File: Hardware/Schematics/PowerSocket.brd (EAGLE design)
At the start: 100 x 80 mm, 60 parts, among them U1 ESP-32S

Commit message: Made relay and amperemeter breakout board.
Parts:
- removed R3, R4, R9: 100, rcl:R0805
- added D2, D3, D4: (no value), diode:DO-214AC
- added Q4, Q5, Q6: (no value), adafruit:SOT23
- moved Q3 247.8 mm to (68.2, 7.90), flipped to the bottom, turned to 270 degrees
- moved Q2 225.5 mm to (72.8, 9.70), flipped to the bottom, turned to 270 degrees
- moved JTAG 185.4 mm to (80.8, 2.73), turned to 180 degrees
- moved R29 163.1 mm to (63.2, 12.4), flipped to the bottom, turned to 180 degrees
- moved U$1 158.8 mm to (62.2, 13.4), turned to 90 degrees
- moved R27 158.3 mm to (63.1, 7.47), flipped to the bottom, turned to 180 degrees
- moved R25 156.4 mm to (63.3, 17.3), flipped to the bottom, turned to 180 degrees
- moved R30 153.5 mm to (58.1, 11.2), flipped to the bottom, turned to 270 degrees
- moved R26 150.1 mm to (58.1, 16.2), flipped to the bottom, turned to 270 degrees
- moved R28 149.3 mm to (58.0, 6.30), flipped to the bottom, turned to 270 degrees
- moved C8 149.1 mm to (61.6, 27.6), flipped to the bottom, turned to 270 degrees
- moved C7 145.2 mm to (63.6, 27.5), flipped to the bottom, turned to 90 degrees
- moved C10 142.1 mm to (41.3, 28.0), flipped to the bottom, turned to 270 degrees
- moved C2 139.5 mm to (75.3, 22.7), flipped to the bottom, turned to 90 degrees
- moved C9 138.3 mm to (43.5, 28.1), flipped to the bottom, turned to 90 degrees
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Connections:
- removed net N$15: Q2.2, U$4.COIL1, U$5.COIL1
- removed net N$16: Q3.1, R9.1
- removed net N$18: Q3.2, U$6.COIL1, U$7.COIL1
- new net LED1_SWITCHED: Q5.3, R7.2
- new net LED2_SWITCHED: Q4.3, R20.2
- new net LED3_SWITCHED: Q6.3, R22.2
- new net N$19: U1.38, UART.1
- net AMP1: now also U1.7; no longer U1.6
- net AMP2: now also U1.8; no longer U1.7
- net AMP3: now also U1.9; no longer U1.8
- net FLASH: now also U1.26; no longer U1.10
- net GATE1: now also Q1.1, U1.10; no longer R3.2, U1.25
- net GATE2: now also Q2.1, U1.11; no longer R4.2, U1.26
- net GATE3: now also Q3.1, U1.12; no longer R9.2, U1.37
- net GND: now also Q1.2, Q2.2, Q3.2, Q4.2, Q5.2, Q6.2; no longer U$2.COIL0, U$3.COIL0, U$4.COIL0, U$5.COIL0, U$6.COIL0, U$7.COIL0, U1.38, UART.1
- net LED1: now also Q5.1; no longer R7.2
- net LED2: now also Q4.1; no longer R20.2
- net LED3: now also Q6.1; no longer R22.2
- net N$1: now also D4.A, Q1.3, U$2.COIL0, U$3.COIL0; no longer Q1.1, R3.1
- net N$14: now also D2.A, Q2.3, U$4.COIL0, U$5.COIL0; no longer Q2.1, R4.1
- net N$6: now also D3.A, Q3.3, U$6.COIL0, U$7.COIL0; no longer Q1.2, U$2.COIL1, U$3.COIL1
- net PHASE1: now also U$2.SWCLOSED; no longer U$2.SWOPEN
- net PHASE2: now also U$4.SWCLOSED; no longer U$4.SWOPEN
- net PHASE3: now also U$6.SWCLOSED; no longer U$6.SWOPEN
- net VCC: now also D2.C, D3.C, D4.C, U$2.COIL1, U$3.COIL1, U$4.COIL1, U$5.COIL1, U$6.COIL1, U$7.COIL1; no longer Q1.3, Q2.3, Q3.3
- net VOLTMETER: now also U1.6; no longer U1.11
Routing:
- net PHASE: track 0.00 -> 96.0 mm
- net NULL: track 0.00 -> 87.5 mm
- net N$15: track 0.00 -> 53.9 mm
- net N$16: track 0.00 -> 37.3 mm
- net +5V: track 0.00 -> 33.9 mm
- net GND: track 0.00 -> 20.9 mm
- net N$18: track 0.00 -> 8.40 mm
- net N$21: track 0.00 -> 8.30 mm
- net N$20: track 0.00 -> 8.00 mm
- net N$17: track 0.00 -> 6.38 mm
- net N$23: track 0.00 -> 6.30 mm
- net N$25: track 0.00 -> 6.10 mm
- net N$8: track 0.00 -> 5.97 mm
- net N$22: track 0.00 -> 5.90 mm
- net NULL_: track 0.00 -> 5.89 mm
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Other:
- outline, holes or cut-outs redrawn

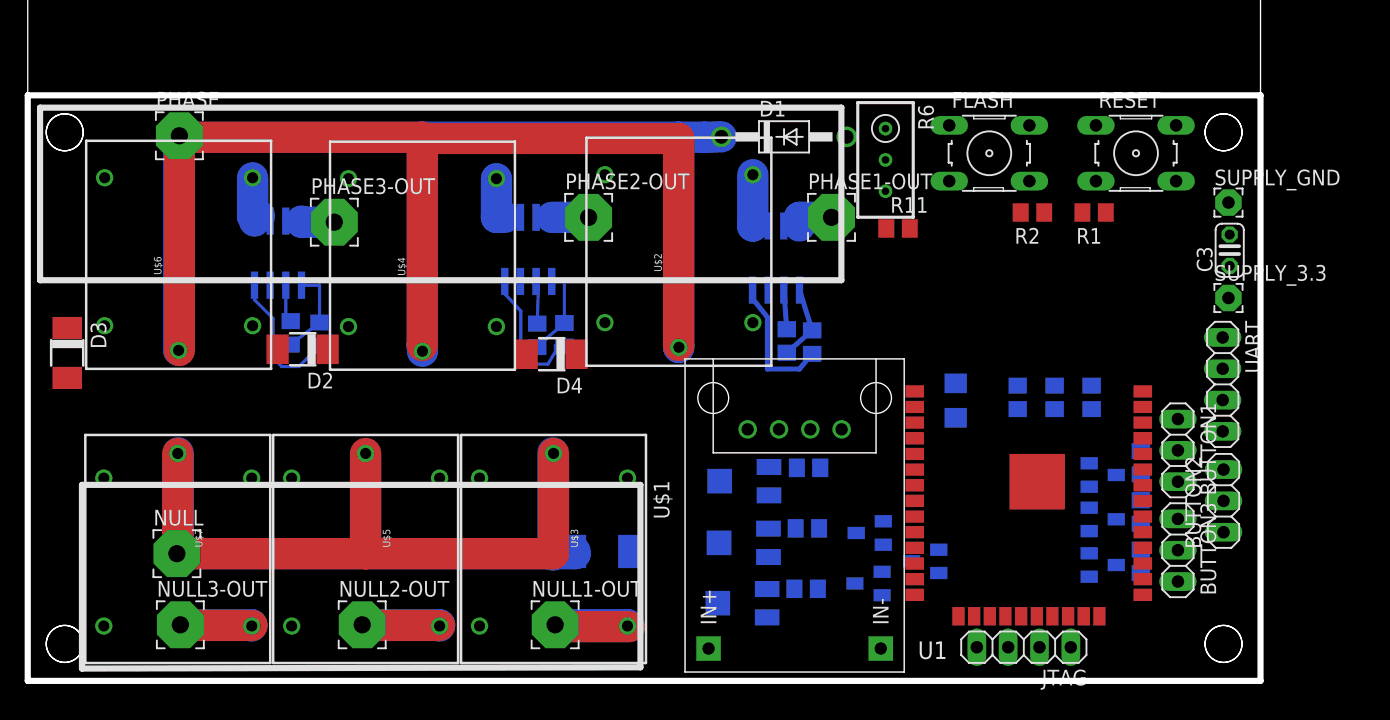
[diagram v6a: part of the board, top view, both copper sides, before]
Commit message: Routed power socket board.
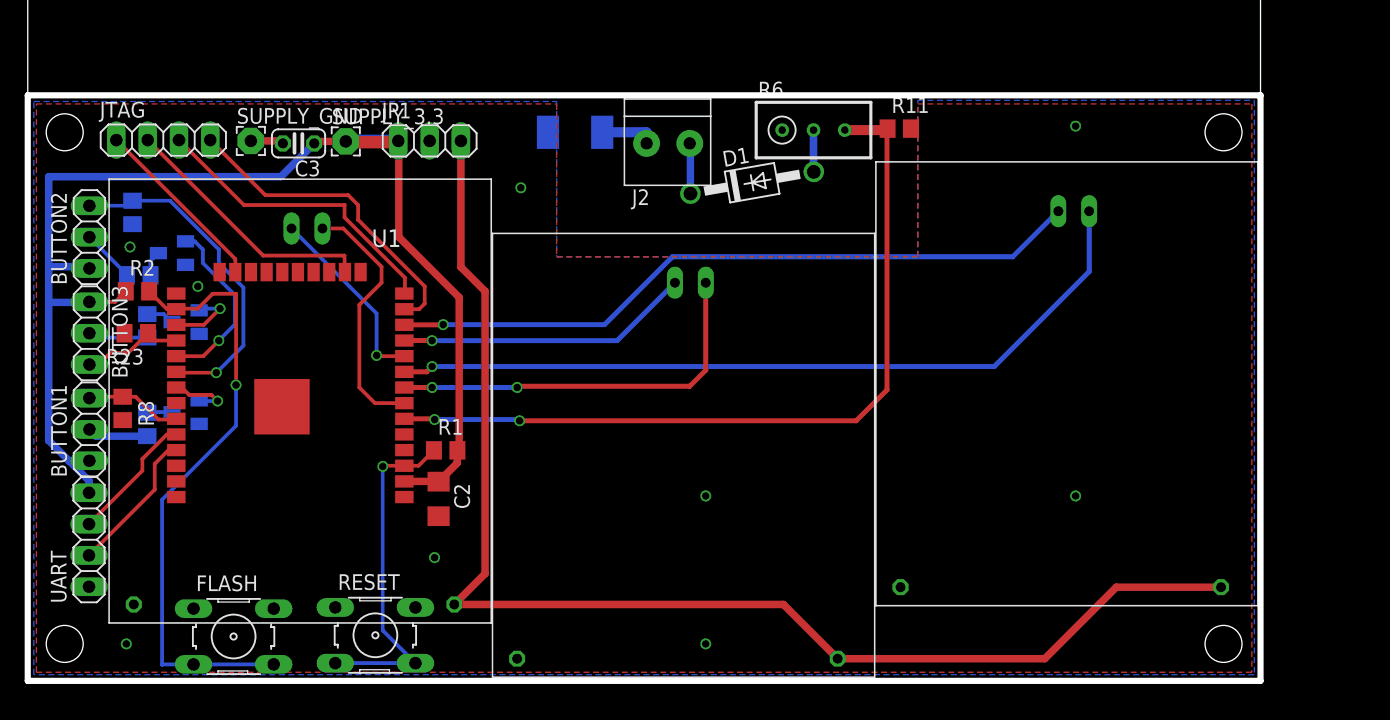
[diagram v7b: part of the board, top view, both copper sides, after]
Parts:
- removed AMP1, AMP2, AMP3: ACS712-LC, allegro-2:SOIC8
- removed C1, C7, C9: 100nF, rcl:C0805
- removed C10, C4, C8: 470nF, rcl:C0805
- removed D2, D3, D4: (no value), diode:DO-214AC
- removed NULL, NULL1-OUT, NULL2-OUT, NULL3-OUT, PHASE, PHASE1-OUT, PHASE2-OUT, PHASE3-OUT: -, wirepad:3,81/1,4
- removed Q1, Q2, Q3: (no value), adafruit:SOT23
- removed R25, R27, R29: 10K, rcl:R0805
- removed R26, R28, R30: 10K, rcl:RTRIM5X
- removed U$1: DC-DC-STEP-UP-5V, diy-modules:DC-DC-STEP-UP-5V
- removed U$5, U$6, U$7: RELAYPTH, SRD-05VDC-SL-C:SRD-05VDC-SL-C
- added J2: 1X2-3.5MM, adafruit:1X2-3.5MM
- added JP1: (no value), pinhead:1X03
- U$2, U$3, U$4: value RELAYPTH -> RELAY_BOARD; device SRD-05VDC-SL-C:SRD-05VDC-SL-C -> PowerSocket:RELAY_BOARD
- moved BUTTON2 94.5 mm to (5.00, 36.0)
- moved UART 92.8 mm to (4.97, 11.4), turned to 90 degrees
- moved BUTTON3 90.0 mm to (5.00, 28.2)
- moved BUTTON1 88.3 mm to (5.00, 20.4), turned to 90 degrees
- moved R20 83.5 mm to (9.00, 32.9), turned to 180 degrees
- moved R22 82.8 mm to (9.70, 28.8), turned to 90 degrees
- moved JTAG 81.0 mm to (11.0, 43.9), turned to 0 degrees
- moved R7 80.7 mm to (9.70, 20.8), turned to 90 degrees
- moved SUPPLY_GND 79.5 mm to (18.1, 43.8)
- moved R8 78.6 mm to (7.70, 22.1), flipped to the top, turned to 270 degrees
- moved Q4 78.5 mm to (11.7, 34.7), turned to 270 degrees
- moved Q6 77.0 mm to (12.8, 29.1), turned to 270 degrees
- moved R21 76.3 mm to (8.50, 38.0), turned to 270 degrees
- moved C3 76.0 mm to (22.0, 43.6), turned to 180 degrees
- moved Q5 74.6 mm to (12.8, 21.8), turned to 270 degrees
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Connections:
- removed net N$1: D4.A, Q1.3, U$2.COIL0, U$3.COIL0
- removed net N$10: AMP3.3, AMP3.4, PHASE3-OUT.1
- removed net N$12: AMP2.3, AMP2.4, PHASE2-OUT.1
- removed net N$13: AMP2.6, C10.1
- removed net N$14: D2.A, Q2.3, U$4.COIL0, U$5.COIL0
- removed net N$17: NULL2-OUT.1, U$5.SWOPEN
- removed net N$19: U1.38, UART.1
- removed net N$24: AMP1.6, C8.1
- removed net N$26: AMP3.6, C4.1
- removed net N$27: AMP1.3, AMP1.4, PHASE1-OUT.1
- removed net N$37: AMP3.7, R29.2
- removed net N$39: AMP2.7, R25.2
- removed net N$41: AMP1.7, R27.2
- removed net N$6: D3.A, Q3.3, U$6.COIL0, U$7.COIL0
- removed net N$8: NULL1-OUT.1, U$3.SWOPEN
- removed net NULL_: NULL3-OUT.1, U$7.SWOPEN
- removed net PHASE1: AMP1.1, AMP1.2, U$2.SWCLOSED
- removed net PHASE2: AMP2.1, AMP2.2, U$4.SWCLOSED
- removed net PHASE3: AMP3.1, AMP3.2, U$6.SWCLOSED
- net +5V: now also JP1.3, U$2.+5V, U$3.+5V, U$4.+5V; no longer AMP1.8, AMP2.8, AMP3.8, C1.1, C7.1, C9.1, U$1.5V
- net AMP1: now also U$4.AMP; no longer R27.1, R28.1
- net AMP2: now also U$3.AMP; no longer R25.1, R26.1
- net AMP3: now also U$2.AMP; no longer R29.1, R30.1
- net GATE1: now also U$4.GATE; no longer Q1.1
- net GATE2: now also U$3.GATE; no longer Q2.1
- net GATE3: now also U$2.GATE; no longer Q3.1
- net GND: now also JP1.2, U$2.GND, U$3.GND, U$4.GND, U1.38, UART.1; no longer AMP1.5, AMP2.5, AMP3.5, C1.2, C10.2, C4.2, C7.2, C8.2, C9.2, Q1.2, Q2.2, Q3.2, R26.2, R28.2, R30.2, U$1.D+, U$1.D-, U$1.GND, U$1.IN-
- net NULL: now also J2.1; no longer NULL.1, U$3.SWCOMMON, U$5.SWCOMMON, U$7.SWCOMMON
- net PHASE: now also J2.2; no longer PHASE.1, U$2.SWCOMMON, U$4.SWCOMMON, U$6.SWCOMMON
- net VCC: now also JP1.1; no longer D2.C, D3.C, D4.C, U$1.IN+, U$2.COIL1, U$3.COIL1, U$4.COIL1, U$5.COIL1, U$6.COIL1, U$7.COIL1
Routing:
- net VCC: track 0.00 -> 105.7 mm
- net PHASE: track 96.0 -> 4.07 mm
- net NULL: track 87.5 -> 4.50 mm
- net +5V: track 33.9 -> 105.9 mm
- net VOLTMETER: track 0.00 -> 65.1 mm, vias 0 -> 2
- net AMP3: track 0.00 -> 63.8 mm, vias 0 -> 1
- net GATE3: track 0.00 -> 56.9 mm, vias 0 -> 1
- net N$15: track 53.9 -> 0.00 mm
- net FLASH: track 0.00 -> 49.8 mm, vias 0 -> 1
- net N$16: track 37.3 -> 0.00 mm
- net AMP2: track 0.00 -> 32.1 mm, vias 0 -> 2
- net N$66: track 0.00 -> 28.2 mm, vias 0 -> 1
- net BUTTON2: track 0.00 -> 27.3 mm, vias 0 -> 1
- net N$5: track 0.00 -> 26.2 mm
- net N$4: track 0.00 -> 24.8 mm
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- added copper zone on layer 1, net GND
- added copper zone on layer 16, net GND

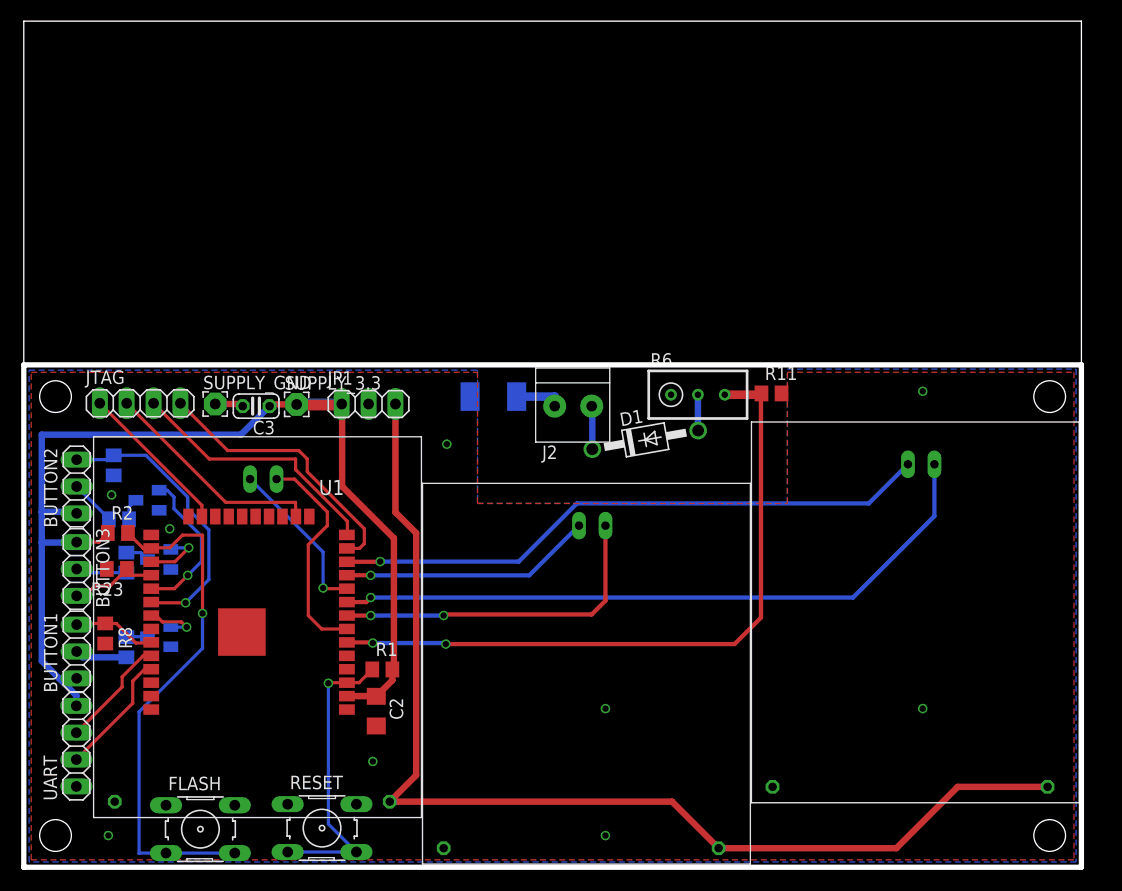
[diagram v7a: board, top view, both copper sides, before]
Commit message: Added panelising readme and lua file.
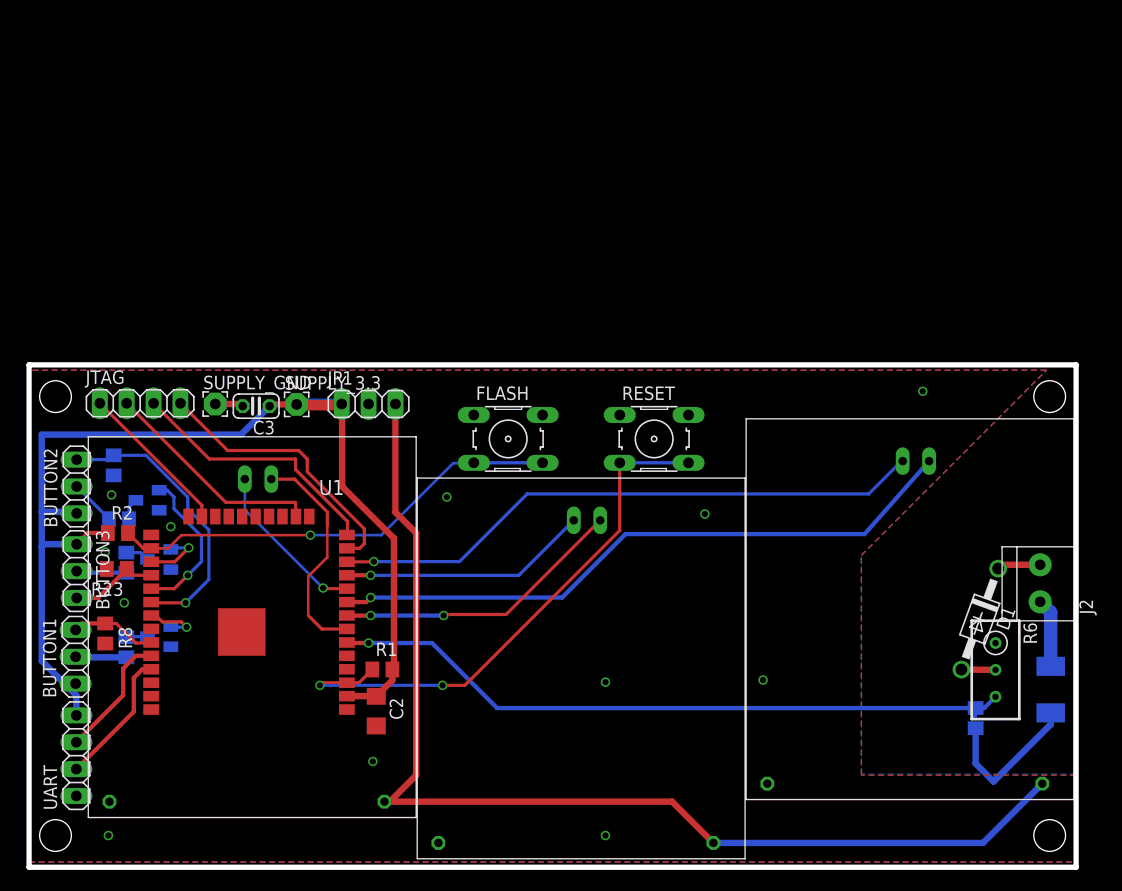
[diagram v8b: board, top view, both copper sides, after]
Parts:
- moved R5 59.5 mm to (97.1, 16.8), turned to 270 degrees
- moved RESET 48.4 mm to (59.6, 40.5)
- moved J2 47.2 mm to (96.1, 26.9), turned to 270 degrees
- moved FLASH 47.0 mm to (45.8, 40.5)
- moved R6 38.3 mm to (91.9, 18.7), turned to 180 degrees
- moved R11 36.3 mm to (90.0, 14.1), flipped to the bottom, turned to 270 degrees
- moved D1 35.9 mm to (90.4, 23.5), turned to 250 degrees
- moved UART 0.90 mm to (4.97, 10.6)
- moved U$3 0.71 mm to (37.2, 0.80)
- moved U$2 0.58 mm to (68.3, 6.40)
- moved BUTTON1 0.51 mm to (4.90, 19.9)
- moved U$4 0.50 mm to (6.10, 4.70)
- moved BUTTON3 0.20 mm to (5.00, 28.0)
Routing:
- net N$66: track 28.2 -> 52.9 mm, vias 1 -> 2
- net GND: track 2.70 -> 17.2 mm, vias 9 -> 12
- net FLASH: track 49.8 -> 43.2 mm
- net AMP2: track 32.1 -> 27.7 mm
- net AMP3: track 63.8 -> 60.8 mm
- net NULL: track 4.50 -> 6.51 mm
- net N$77: track 10.6 -> 12.0 mm
- net N$70: track 11.8 -> 12.9 mm
- net VCC: track 105.7 -> 106.2 mm
- net AMP1: track 20.8 -> 21.3 mm
- net VOLTMETER: track 65.1 -> 65.2 mm, vias 2 -> 1
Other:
- board size 100 x 80 mm -> 99 x 47.5 mm
